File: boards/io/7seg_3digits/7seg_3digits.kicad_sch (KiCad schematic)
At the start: 14 parts, among them J1 Conn_02x06_Top_Bottom, J2 Conn_PIC_ICSP_ICD, SW1 SW_DIP_x02, U1 PIC16F1933T-I/SO, U2 OSL30561-LRA

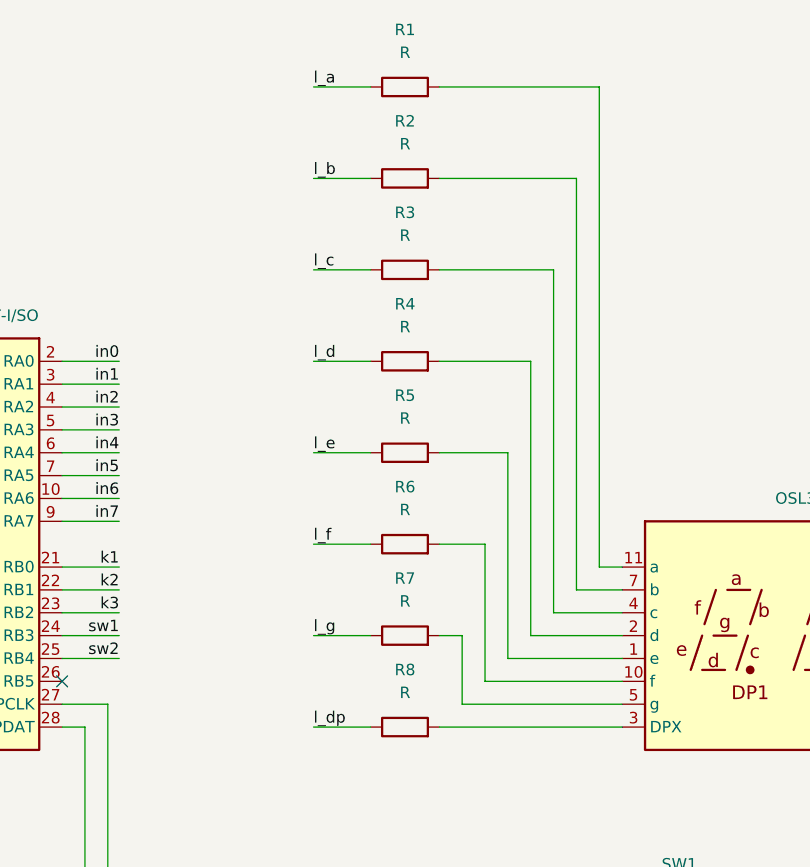
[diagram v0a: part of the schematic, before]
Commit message: set resistor values
* 7seg_1digit
* 7seg_3digits
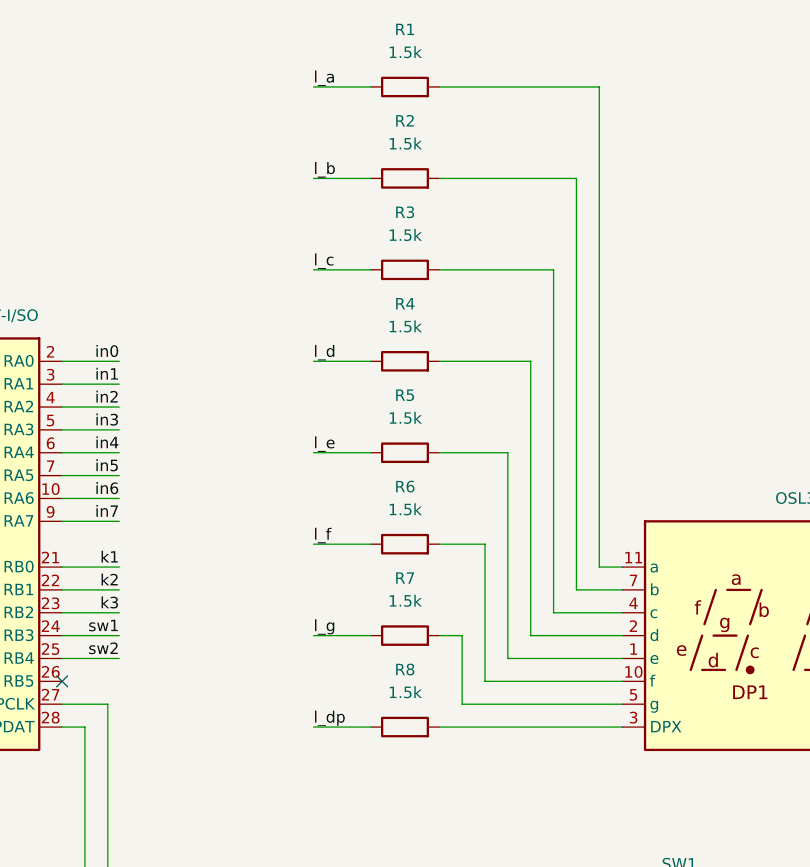
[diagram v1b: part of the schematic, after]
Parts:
- R1, R2, R3, R4, R5, R6, R7, R8: value R -> 1.5k
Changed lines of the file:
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@@
     (in_bom yes) (on_board yes) (fields_autoplaced)
     (property "Reference" "R4" (id 0) (at 193.04 57.15 90))
-    (property "Value" "R" (id 1) (at 193.04 59.69 90))
+    (property "Value" "1.5k" (id 1) (at 193.04 59.69 90))
     (property "Footprint" "Resistor_SMD:R_0805_2012Metric_Pad1.20x1.40mm_HandSolder" (id 2) (at 193.04 65.278 90)
       (effects (font (size 1.27 1.27)) hide)
@@
     (in_bom yes) (on_board yes) (fields_autoplaced)
     (property "Reference" "R2" (id 0) (at 193.04 36.83 90))
-    (property "Value" "R" (id 1) (at 193.04 39.37 90))
+    (property "Value" "1.5k" (id 1) (at 193.04 39.37 90))
     (property "Footprint" "Resistor_SMD:R_0805_2012Metric_Pad1.20x1.40mm_HandSolder" (id 2) (at 193.04 44.958 90)
       (effects (font (size 1.27 1.27)) hide)
@@
     (in_bom yes) (on_board yes) (fields_autoplaced)
     (property "Reference" "R1" (id 0) (at 193.04 26.67 90))
-    (property "Value" "R" (id 1) (at 193.04 29.21 90))
+    (property "Value" "1.5k" (id 1) (at 193.04 29.21 90))
     (property "Footprint" "Resistor_SMD:R_0805_2012Metric_Pad1.20x1.40mm_HandSolder" (id 2) (at 193.04 34.798 90)
       (effects (font (size 1.27 1.27)) hide)
@@
     (in_bom yes) (on_board yes) (fields_autoplaced)
     (property "Reference" "R7" (id 0) (at 193.04 87.63 90))
-    (property "Value" "R" (id 1) (at 193.04 90.17 90))
+    (property "Value" "1.5k" (id 1) (at 193.04 90.17 90))
     (property "Footprint" "Resistor_SMD:R_0805_2012Metric_Pad1.20x1.40mm_HandSolder" (id 2) (at 193.04 95.758 90)
       (effects (font (size 1.27 1.27)) hide)
@@
     (in_bom yes) (on_board yes) (fields_autoplaced)
     (property "Reference" "R8" (id 0) (at 193.04 97.79 90))
-    (property "Value" "R" (id 1) (at 193.04 100.33 90))
+    (property "Value" "1.5k" (id 1) (at 193.04 100.33 90))
     (property "Footprint" "Resistor_SMD:R_0805_2012Metric_Pad1.20x1.40mm_HandSolder" (id 2) (at 193.04 105.918 90)
       (effects (font (size 1.27 1.27)) hide)
@@
     (in_bom yes) (on_board yes) (fields_autoplaced)
     (property "Reference" "R5" (id 0) (at 193.04 67.31 90))
-    (property "Value" "R" (id 1) (at 193.04 69.85 90))
+    (property "Value" "1.5k" (id 1) (at 193.04 69.85 90))
     (property "Footprint" "Resistor_SMD:R_0805_2012Metric_Pad1.20x1.40mm_HandSolder" (id 2) (at 193.04 75.438 90)
       (effects (font (size 1.27 1.27)) hide)
@@
     (in_bom yes) (on_board yes) (fields_autoplaced)
     (property "Reference" "R6" (id 0) (at 193.04 77.47 90))
-    (property "Value" "R" (id 1) (at 193.04 80.01 90))
+    (property "Value" "1.5k" (id 1) (at 193.04 80.01 90))
     (property "Footprint" "Resistor_SMD:R_0805_2012Metric_Pad1.20x1.40mm_HandSolder" (id 2) (at 193.04 85.598 90)
       (effects (font (size 1.27 1.27)) hide)
@@
     (in_bom yes) (on_board yes) (fields_autoplaced)
     (property "Reference" "R3" (id 0) (at 193.04 46.99 90))
-    (property "Value" "R" (id 1) (at 193.04 49.53 90))
+    (property "Value" "1.5k" (id 1) (at 193.04 49.53 90))
     (property "Footprint" "Resistor_SMD:R_0805_2012Metric_Pad1.20x1.40mm_HandSolder" (id 2) (at 193.04 55.118 90)
       (effects (font (size 1.27 1.27)) hide)
@@
     )
     (path "/5a3529d8-9c5d-43e6-a178-5cba6ef3c8e8"
-      (reference "R1") (unit 1) (value "R") (footprint "Resistor_SMD:R_0805_2012Metric_Pad1.20x1.40mm_HandSolder")
+      (reference "R1") (unit 1) (value "1.5k") (footprint "Resistor_SMD:R_0805_2012Metric_Pad1.20x1.40mm_HandSolder")
     )
     (path "/58bbea50-236e-4f3f-8029-d91da3c49e38"
-      (reference "R2") (unit 1) (value "R") (footprint "Resistor_SMD:R_0805_2012Metric_Pad1.20x1.40mm_HandSolder")
+      (reference "R2") (unit 1) (value "1.5k") (footprint "Resistor_SMD:R_0805_2012Metric_Pad1.20x1.40mm_HandSolder")
     )
     (path "/db9c3f38-9173-4705-a62a-3fda91a6d556"
-      (reference "R3") (unit 1) (value "R") (footprint "Resistor_SMD:R_0805_2012Metric_Pad1.20x1.40mm_HandSolder")
+      (reference "R3") (unit 1) (value "1.5k") (footprint "Resistor_SMD:R_0805_2012Metric_Pad1.20x1.40mm_HandSolder")
     )
     (path "/3c55df7e-b924-4ec0-9e70-e05160af0dd5"
-      (reference "R4") (unit 1) (value "R") (footprint "Resistor_SMD:R_0805_2012Metric_Pad1.20x1.40mm_HandSolder")
+      (reference "R4") (unit 1) (value "1.5k") (footprint "Resistor_SMD:R_0805_2012Metric_Pad1.20x1.40mm_HandSolder")
     )
     (path "/897ebac6-d664-4746-b634-be10196423bb"
-      (reference "R5") (unit 1) (value "R") (footprint "Resistor_SMD:R_0805_2012Metric_Pad1.20x1.40mm_HandSolder")
+      (reference "R5") (unit 1) (value "1.5k") (footprint "Resistor_SMD:R_0805_2012Metric_Pad1.20x1.40mm_HandSolder")
     )
     (path "/a660d817-3c20-45af-b359-cdf61f39acc9"
-      (reference "R6") (unit 1) (value "R") (footprint "Resistor_SMD:R_0805_2012Metric_Pad1.20x1.40mm_HandSolder")
+      (reference "R6") (unit 1) (value "1.5k") (footprint "Resistor_SMD:R_0805_2012Metric_Pad1.20x1.40mm_HandSolder")
     )
     (path "/5fcbc013-0b4a-487a-bbec-cc4c01132478"
-      (reference "R7") (unit 1) (value "R") (footprint "Resistor_SMD:R_0805_2012Metric_Pad1.20x1.40mm_HandSolder")
+      (reference "R7") (unit 1) (value "1.5k") (footprint "Resistor_SMD:R_0805_2012Metric_Pad1.20x1.40mm_HandSolder")
     )
     (path "/872cd9ea-063b-4d8e-aa3b-f8c6273c5ec8"
-      (reference "R8") (unit 1) (value "R") (footprint "Resistor_SMD:R_0805_2012Metric_Pad1.20x1.40mm_HandSolder")
+      (reference "R8") (unit 1) (value "1.5k") (footprint "Resistor_SMD:R_0805_2012Metric_Pad1.20x1.40mm_HandSolder")
     )
     (path "/d239e019-6470-4175-aab2-567880a09767"
